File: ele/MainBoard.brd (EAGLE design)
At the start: 100.1 x 58.3 mm, 51 parts, among them X1 M8, X2 M8, X4 POWER_IN

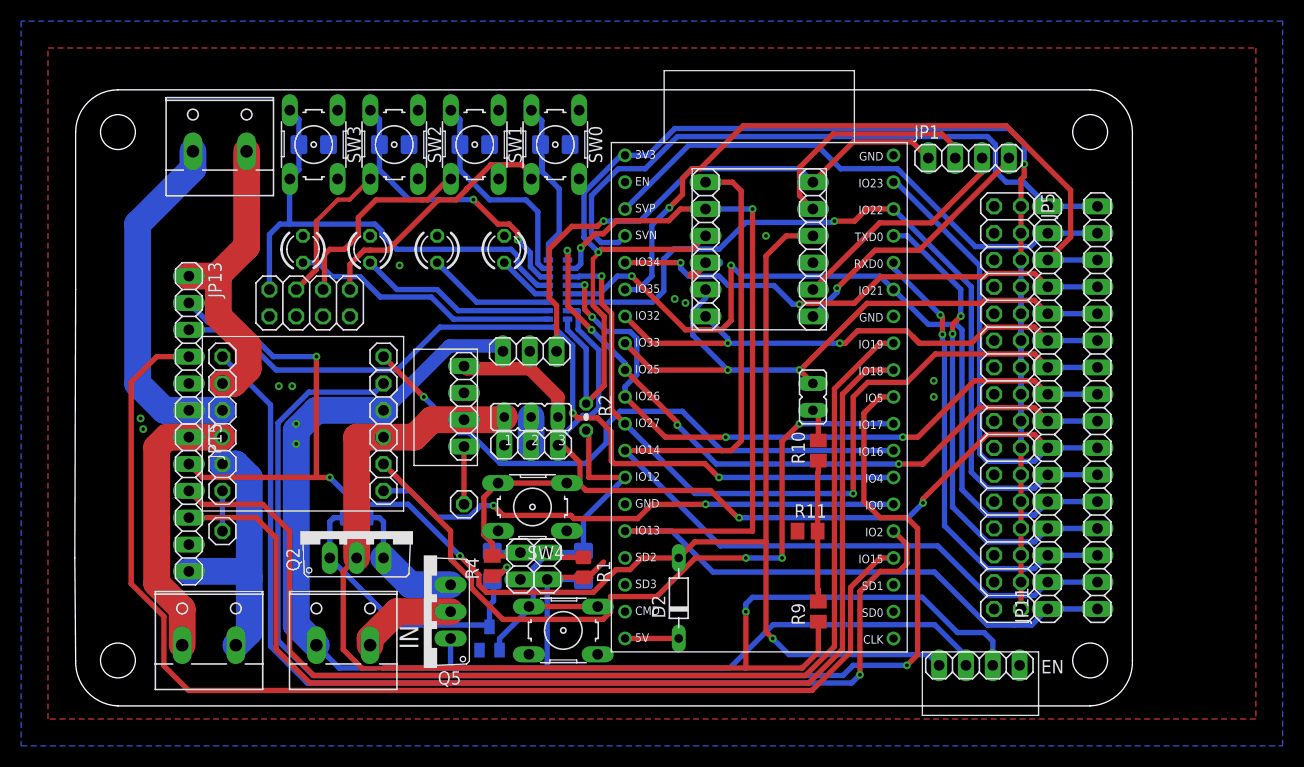
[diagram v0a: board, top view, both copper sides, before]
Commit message: ele: MainBoard - Add CC BY-SA license, fix pinheads position
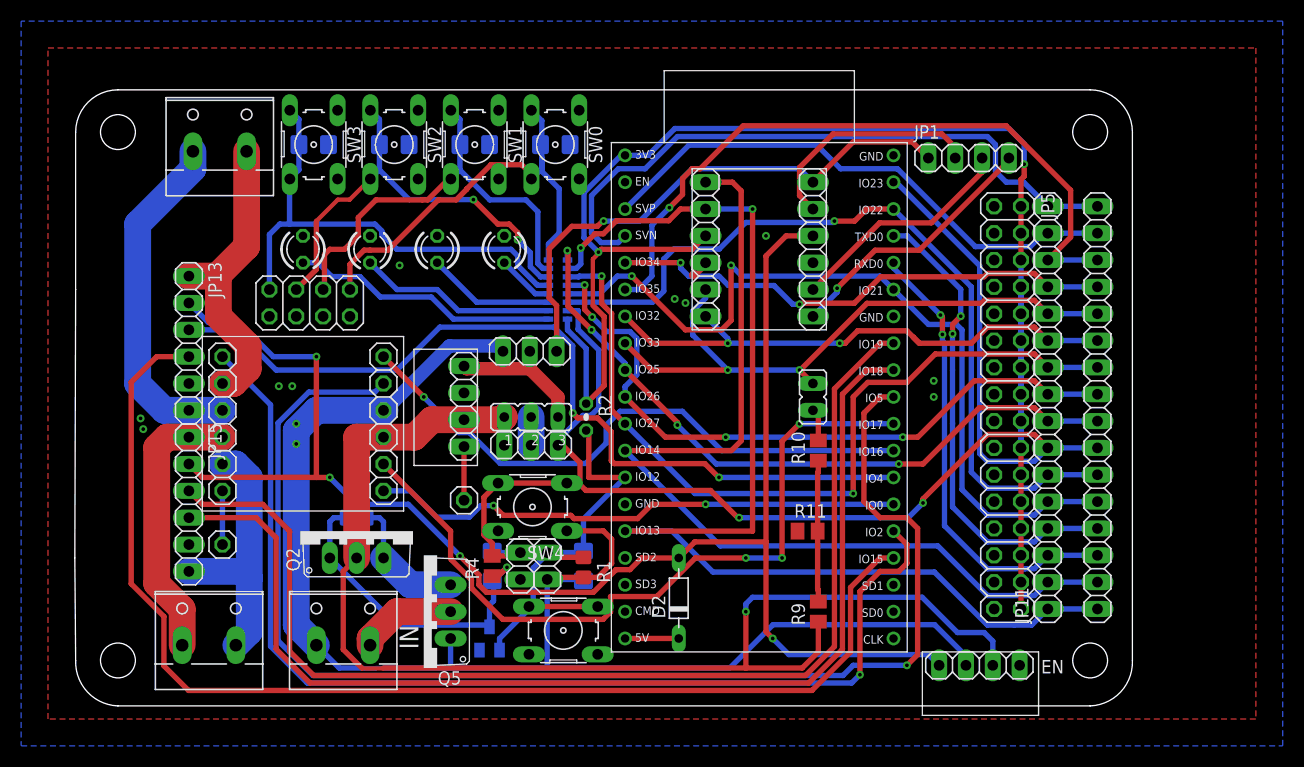
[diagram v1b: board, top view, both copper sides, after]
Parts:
- moved JP30 1.27 mm to (8.89, 14.0)
- moved JP10 0.38 mm to (31.8, 18.2)
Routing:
- net GND: track 138.2 -> 143.8 mm
- net N$1: track 3.81 -> 5.08 mm
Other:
- outline, holes or cut-outs redrawn
- board text added: "Battery"
- board text removed: "Batteri"

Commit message: condenser
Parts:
- added C7: (no value), rcl:E5-10,5
- added D3: (no value), diode:F126Z12
- moved JP2 3.31 mm to (61.5, 27.7), turned to 90 degrees
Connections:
- net N$7 renamed IO9_NC2
- net GND: now also C7.-, D3.A
- net VCC: now also C7.+, D3.C
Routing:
- net VCC: track 118.6 -> 130.5 mm
- net GPIO33: track 60.3 -> 64.2 mm
- net N$2: track 3.07 -> 6.14 mm
- net SW2: track 42.6 -> 44.3 mm, vias 2 -> 0
- net +5V: track 146.3 -> 147.5 mm
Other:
- board text added: "1"
- board text added: "13"
- board text added: "14"
- board text added: "21"
- board text added: "22"
- board text added: "23"
- board text added: "25"
- board text added: "26"
- board text added: "27"
- board text added: "3"
- board text added: "32"
- board text added: "33"
- board text added: "34"
- board text added: "35"
- board text added: "36"
- board text added: "39"
- board text removed: "IO1"
- board text removed: "IO21"
- board text removed: "IO22"
- board text removed: "IO23"
- board text removed: "IO25"
- board text removed: "IO26"
- board text removed: "IO27"
- board text removed: "IO3"
- board text removed: "IO32"
- board text removed: "IO33"
- board text removed: "IO34"
- board text removed: "IO35"
- board text removed: "IO36"
- board text removed: "IO39"

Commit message: ladeni
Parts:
- added C6: (no value), rcl:E5-10,5
- added JP7: (no value), pinhead:1X04/90
- moved Q2 0.89 mm to (21.6, 14.4)
- moved JP2 0.51 mm to (62.0, 27.7)
- moved SW5 0.13 mm to (41.1, 5.97)
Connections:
- net +5V: now also JP7.1, JP7.2, JP7.3, JP7.4
- net GND: now also C6.-
- net VCC: now also C6.+
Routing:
- net GND: track 143.8 -> 117.8 mm, vias 12 -> 15
- net +5V: track 147.5 -> 163.7 mm, vias 4 -> 5
- net GPIO14-5V: track 51.7 -> 50.9 mm
- net START_GATE1: track 31.2 -> 31.9 mm, vias 1 -> 2
- net GPIO35: track 67.0 -> 67.8 mm
- net GPIO33: track 64.2 -> 63.4 mm
- net PWM2: track 124.7 -> 125.4 mm
- net SLEEP: track 103.8 -> 104.5 mm
- net GPIO13-5V: track 22.1 -> 21.5 mm
- net BAT_PROT1: track 12.6 -> 13.1 mm
- net N$2: track 6.14 -> 5.63 mm
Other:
- board text added: "GPIO13"
- board text added: "GPIO15"
- board text added: "IO32"
- board text added: "IO33"
